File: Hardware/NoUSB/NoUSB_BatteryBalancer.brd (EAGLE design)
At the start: 93.6 x 20.1 mm, 94 parts, among them IC1 OP-AMP, J2 ISP, U1 TAP_POINT, U10 MCP1755, U11 AD7280A, U12 ATMEGA328P_TQFP, U13 CH340C, U2 TAP_POINT, U3 TAP_POINT, U4 TAP_POINT, U5 TAP_POINT, Y1 16MHz

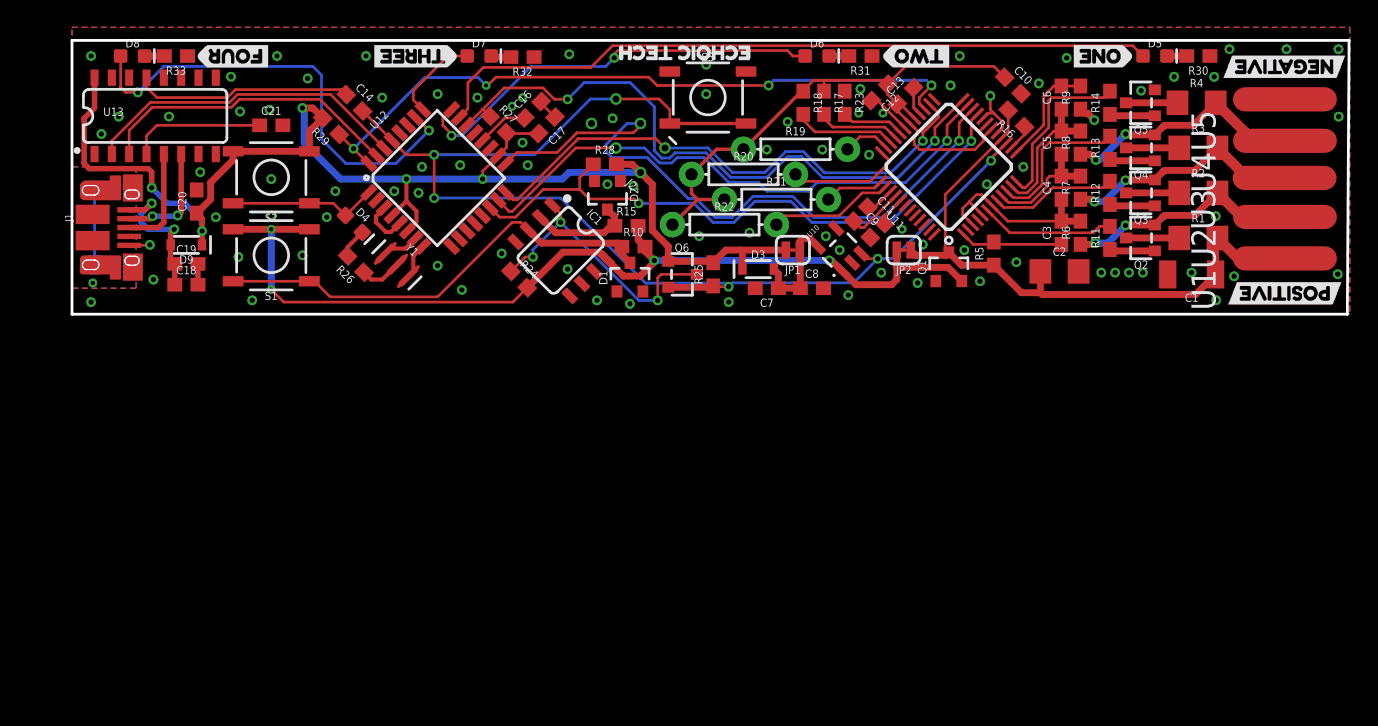
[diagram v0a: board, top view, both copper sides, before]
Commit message: Panelized and ordered test board
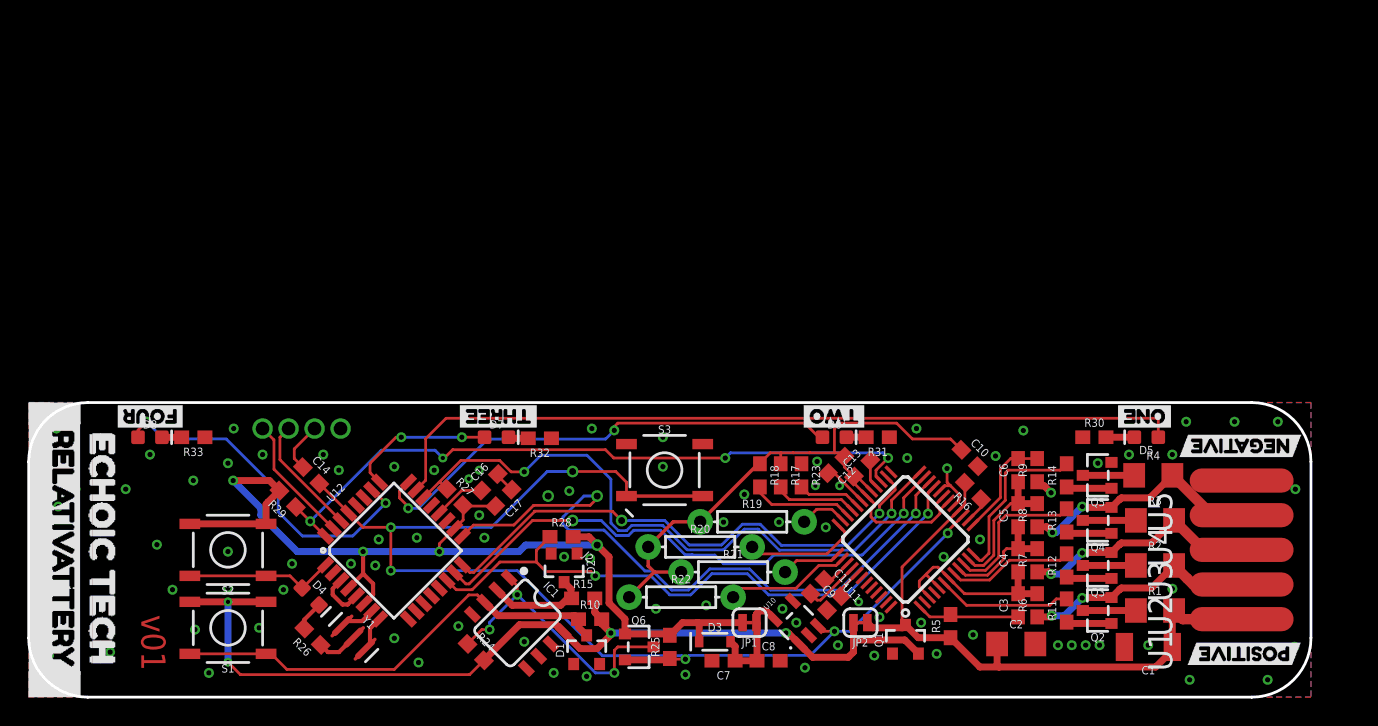
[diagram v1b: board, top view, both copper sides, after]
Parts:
- removed C18, C20: 0.1uF, SparkFun-Capacitors:0603
- removed C19: 1.0uF, SparkFun-Capacitors:0603
- removed C21: 10nF, SparkFun-Capacitors:0603
- removed D9: 3A/10V/280mV, SparkFun-DiscreteSemi:SOD-323
- removed J1: (no value), SparkFun-Connectors:USB-MICROB-PTH-MILL
- removed U13: CH340C, SparkFun-IC-Comms:SO016
- added U$9: (no value), buzzard_labels_echoic:ECHOIC_TECH4
- U$3: device buzzard_labels_0:ONE3 -> buzzard_labels_echoic:TWO2
- U$4: device buzzard_labels_0:TWO4 -> buzzard_labels_echoic:THREE3
- U$5: device buzzard_labels_0:THREE6 -> buzzard_labels_echoic:FOUR4
- U$6: device buzzard_labels_0:FOUR5 -> buzzard_labels_echoic:RELATIVATTERY5
- U$7: device buzzard_labels_0:ECHOIC_TECH7 -> buzzard_labels_echoic:ONE1
- moved U$7 40.4 mm to (87.4, 22.5)
- moved U$4 40.1 mm to (40.9, 22.5)
- moved U$5 32.9 mm to (15.0, 22.5)
- moved U$3 32.7 mm to (64.9, 22.5)
- moved U$6 30.3 mm to (5.71, 22.9), turned to 270 degrees
- moved R30 29.0 mm to (81.3, 21.0), turned to 0 degrees
- moved U5 28.1 mm to (92.1, 17.8)
- moved U$2 28.0 mm to (96.5, 20.3)
- moved D6 28.0 mm to (62.2, 21.0)
- moved D7 28.0 mm to (37.5, 21.0)
- moved R31 28.0 mm to (65.4, 21.0)
- moved R32 28.0 mm to (40.6, 20.9)
- moved D8 28.0 mm to (12.1, 21.0)
- moved R33 28.0 mm to (15.2, 21.0)
- moved D5 27.9 mm to (85.1, 21.0), turned to 180 degrees
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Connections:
- removed net D+: J1.D+, U13.5
- removed net D-: J1.D-, U13.6
- removed net N$38: C21.1, U13.4
- removed net SHLD: J1.SHIELD, J1.SHIELD10, J1.SHIELD2, J1.SHIELD3, J1.SHIELD4, J1.SHIELD5, J1.SHIELD6, J1.SHIELD7, J1.SHIELD8, J1.SHIELD9
- removed net USBVCC: C18.1, C19.1, D9.A, J1.VBUS
- net !DTR: no longer U13.13
- net GND: no longer C18.2, C19.2, C20.2, C21.2, J1.GND, U13.1
- net RX-I: no longer U13.2
- net TX-O: no longer U13.3
- net VCC: no longer C20.1, D9.C, U13.16
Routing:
- net VCC: track 97.6 -> 73.7 mm, vias 5 -> 3
- net RX-I: track 24.0 -> 8.87 mm, vias 0 -> 1
- net TX-O: track 22.5 -> 9.47 mm, vias 0 -> 1
- net !DTR: track 16.0 -> 3.71 mm, vias 0 -> 1
- net USBVCC: track 10.5 -> 0.00 mm, vias 2 -> 0
- net N$38: track 9.96 -> 0.00 mm
- net D-: track 8.26 -> 0.00 mm, vias 2 -> 0
- net LED4: track 33.9 -> 25.7 mm
- net D+: track 7.70 -> 0.00 mm
- net LED1: track 53.7 -> 59.7 mm
- net SHLD: track 5.46 -> 0.00 mm
- net LED2: track 31.3 -> 36.0 mm
- net LED3: track 6.68 -> 10.9 mm, vias 0 -> 2
- net GND: track 24.5 -> 21.5 mm, vias 89 -> 88
- net VREG: track 49.4 -> 52.0 mm
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- removed copper zone on layer 1, net SHLD
- removed copper zone on layer 16, net SHLD
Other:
- board size 93.6 x 20.1 mm -> 94 x 21.6 mm
- board text added: "v01"
